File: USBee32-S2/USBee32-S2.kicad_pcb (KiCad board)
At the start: 4 copper layers, 27.9 x 68.4 mm, 52 parts, among them IC1 IP4220CZ6, J1 USB_A, J2 TYPE-C-31-M-12, J3 Conn_01x18_Male, J4 S2B-PH-SM4-TB(LF)(SN), J5 Conn_01x22_Male, SW1 SW_Push, SW2 SW_Push, U1 ESP32-S2-WROOM-ESP32-S2-WROOM, U2 MMBT8050, U3 MMBT8050, U4 MCP73831-2-OT, U5 AMS1117-3.3, U6 CH340C

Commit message: Rotated board
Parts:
- moved J3 76.8 mm to (203.8, 109.0), turned to 270 degrees
- moved J5 76.7 mm to (203.8, 133.8), turned to 270 degrees
- moved REF** 72.7 mm to (201.9, 114.8), turned to 90 degrees
- moved REF** 72.5 mm to (202.1, 124.1), turned to 90 degrees
- moved U1 64.1 mm to (196.2, 121.3), turned to 270 degrees
- moved GND 64.1 mm to (196.2, 120.1), turned to 270 degrees
- moved G1 55.3 mm to (190.1, 121.5), turned to 90 degrees
- moved G*** 46.9 mm to (184.1, 121.5), turned to 90 degrees
- moved R1 38.6 mm to (178.2, 121.4), turned to 90 degrees
- moved D2 35.6 mm to (174.9, 113.9), turned to 0 degrees
- moved C3 35.1 mm to (175.1, 115.9), turned to 0 degrees
- moved C8 34.5 mm to (175.0, 117.7), turned to 180 degrees
- moved C10 34.2 mm to (175.1, 119.4), turned to 180 degrees
- moved U5 31.7 mm to (173.1, 124.9), turned to 270 degrees
- moved R13 30.5 mm to (171.1, 113.9), turned to 180 degrees
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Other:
- board size 27.9 x 68.4 mm -> 68.4 x 27.9 mm

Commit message: Made suggested changes in schematics
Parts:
- removed G***: LOGO, USBee32-S2-Label:usbee32s2-qr
- removed G***: LOGO, USBee32-S2-Label:usbee32s2-fs
- removed G***: LOGO, USBee32-S2-Label:largelabel
- removed G1: LOGO, WS2018:sralogo
- removed GND: SolderWirePad_1x01_SMD_5x10mm, Connector_Wire:SolderWirePad_1x01_SMD_5x10mm
- removed the R11 at (153.1, 124.2)
- removed REF**: OSHW-Logo_5.7x6mm_SilkScreen, Designs:OSHW-Logo_5.7x6mm_SilkScreen
- removed REF**: KiCad-Logo_5mm_SilkScreen, Designs:KiCad-Logo_5mm_SilkScreen
- added R_PROG: 4.7k, Resistor_SMD:R_0603_1608Metric, F.Cu at (182.6, 108.7)
- moved J5 76.7 mm to (192.2, 58.0), turned to 0 degrees
- moved J3 62.6 mm to (167.4, 58.0), turned to 0 degrees
- moved U1 58.1 mm to (179.7, 65.5), turned to 0 degrees
- moved J1 50.1 mm to (188.9, 122.4), turned to 90 degrees
- moved D1 41.7 mm to (187.4, 112.9), turned to 180 degrees
- moved F1 40.4 mm to (187.3, 110.4), turned to 0 degrees
- moved D4 38.3 mm to (186.2, 94.6), turned to 0 degrees
- moved R1 37.8 mm to (179.8, 83.6), turned to 180 degrees
- moved U3 37.7 mm to (183.3, 88.7), turned to 0 degrees
- moved R4 36.6 mm to (185.6, 106.2), turned to 270 degrees
- moved C11 36.2 mm to (185.5, 99.2), turned to 90 degrees
- moved R9 36.1 mm to (185.6, 102.8), turned to 90 degrees
- moved J4 35.2 mm to (179.9, 116.7), turned to 0 degrees
- moved U2 35.0 mm to (182.8, 111.4), turned to 0 degrees
- moved C10 32.8 mm to (177.8, 86.7), turned to 270 degrees
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- renumbered U2 to Q1, U3 to Q2, R12 to R11, R13 to R12, R14 to R13, U4 to U2, U5 to U3, U6 to U4
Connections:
- net /GPIO0 renamed /GPIO_0
- net /GPIO1 renamed /GPIO_1
- net /GPIO10 renamed /GPIO_10
- net /GPIO11 renamed /GPIO_11
- net /GPIO12 renamed /GPIO_12
- net /GPIO13 renamed /GPIO_13
- net /GPIO14 renamed /GPIO_14
- net /GPIO15 renamed /GPIO_15
- net /GPIO16 renamed /GPIO_16
- net /GPIO17 renamed /GPIO_17
- net /GPIO18 renamed /GPIO_18
- net /GPIO19 renamed /GPIO_19
- net /GPIO2 renamed /GPIO_2
- net /GPIO20 renamed /GPIO_20
- net /GPIO21 renamed /GPIO_21
- net /GPIO26 renamed /GPIO_26
- net /GPIO3 renamed /GPIO_3
- net /GPIO33 renamed /GPIO_33
- net /GPIO34 renamed /GPIO_34
- net /GPIO35 renamed /GPIO_35
- net /GPIO36 renamed /GPIO_36
- net /GPIO37 renamed /GPIO_37
- net /GPIO38 renamed /GPIO_38
- net /GPIO39 renamed /GPIO_39
- net /GPIO4 renamed /GPIO_4
- net /GPIO40 renamed /GPIO_40
- net /GPIO41 renamed /GPIO_41
- net /GPIO42 renamed /GPIO_42
- net /GPIO45 renamed /GPIO_45
- net /GPIO46 renamed /GPIO_46
- net /GPIO5 renamed /GPIO_5
- net /GPIO6 renamed /GPIO_6
- net /GPIO7 renamed /GPIO_7
- net /GPIO8 renamed /GPIO_8
- net /GPIO9 renamed /GPIO_9
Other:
- board size 68.4 x 27.9 mm -> 27.9 x 68.4 mm

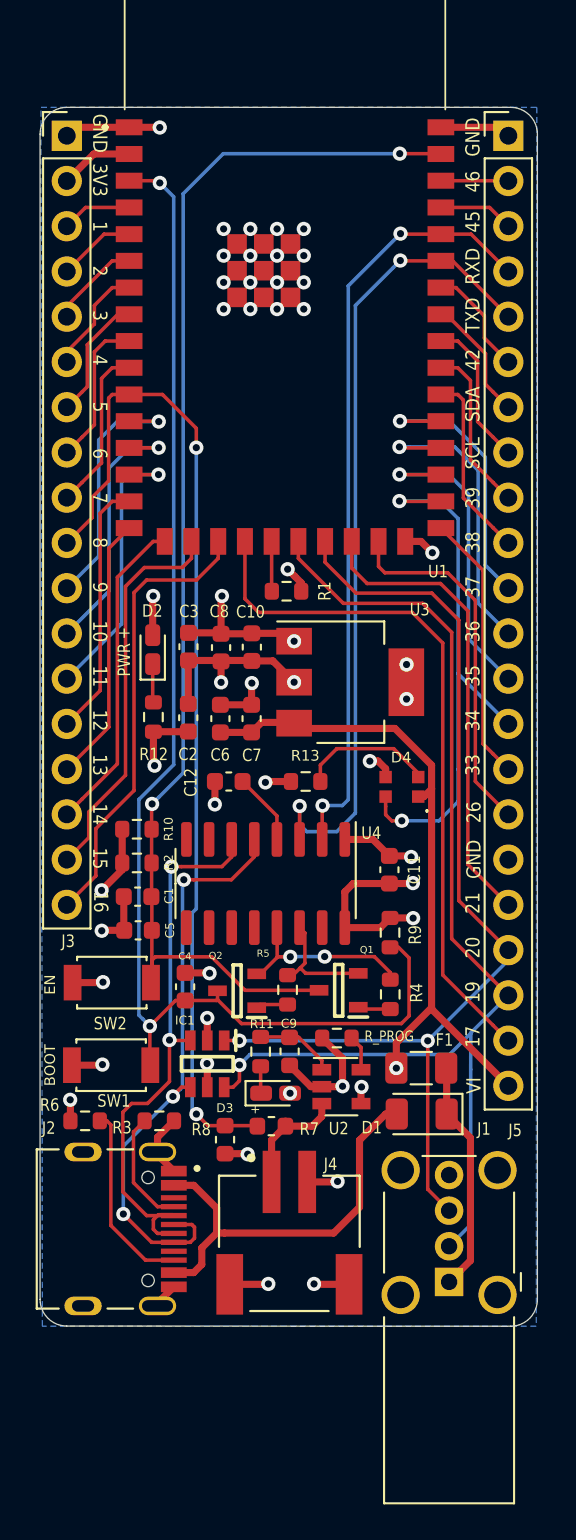
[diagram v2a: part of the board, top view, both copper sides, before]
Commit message: Rotated UsbC and added differential pair
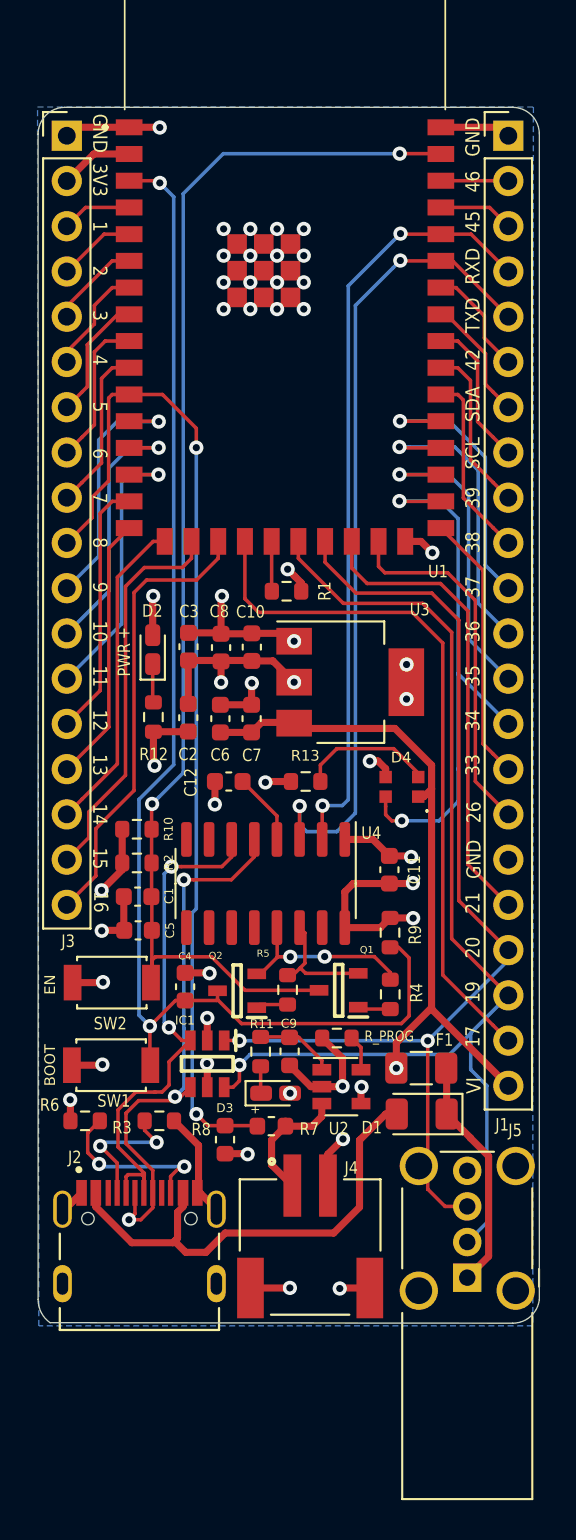
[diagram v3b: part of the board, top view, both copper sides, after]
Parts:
- moved J2 4.41 mm to (171.5, 122.5), turned to 0 degrees
- moved J4 1.18 mm to (181.1, 117.0)
- moved J1 1.05 mm to (189.9, 122.1)
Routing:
- net /VBUSC: track 23.3 -> 27.1 mm
- net GND: track 64.7 -> 68.2 mm
- net /DP1: track 33.5 -> 31.3 mm
- net /DN1: track 32.2 -> 30.0 mm
- net /CC1: track 6.55 -> 7.77 mm, vias 0 -> 2
- net /CC2: track 10.8 -> 9.80 mm, vias 0 -> 2
- net /GPIO_20: track 58.2 -> 59.1 mm
- net +BATT: track 7.86 -> 7.16 mm
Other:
- board size 27.9 x 68.4 mm -> 28.1 x 68.3 mm

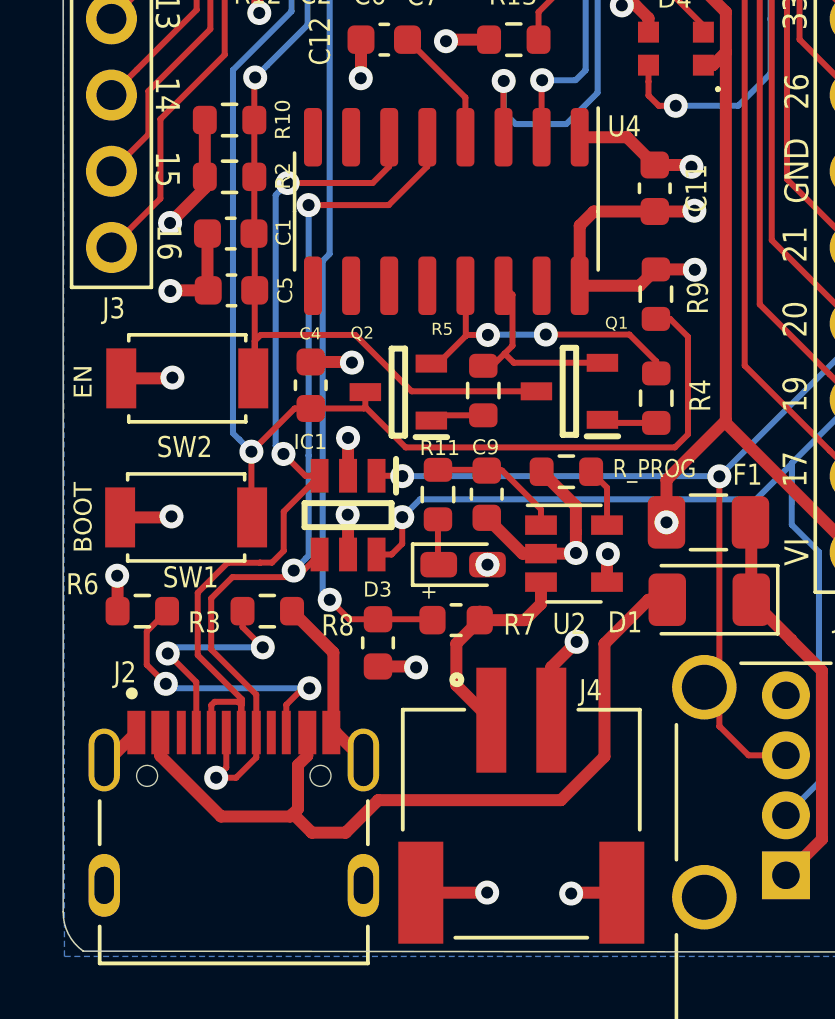
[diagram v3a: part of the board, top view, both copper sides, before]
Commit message: Made minor changes in routing
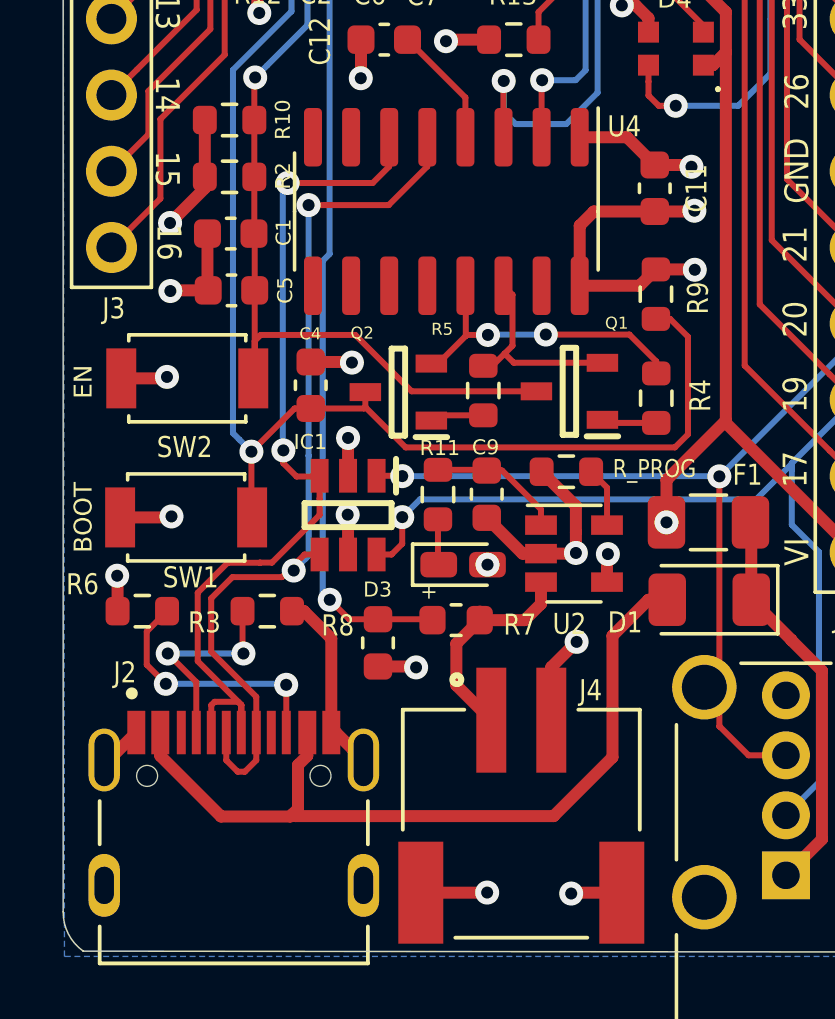
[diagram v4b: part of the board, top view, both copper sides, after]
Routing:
- net /CC2: track 9.80 -> 8.65 mm
- net /DP1: track 31.3 -> 30.3 mm, vias 3 -> 2
- net /CC1: track 7.77 -> 6.98 mm

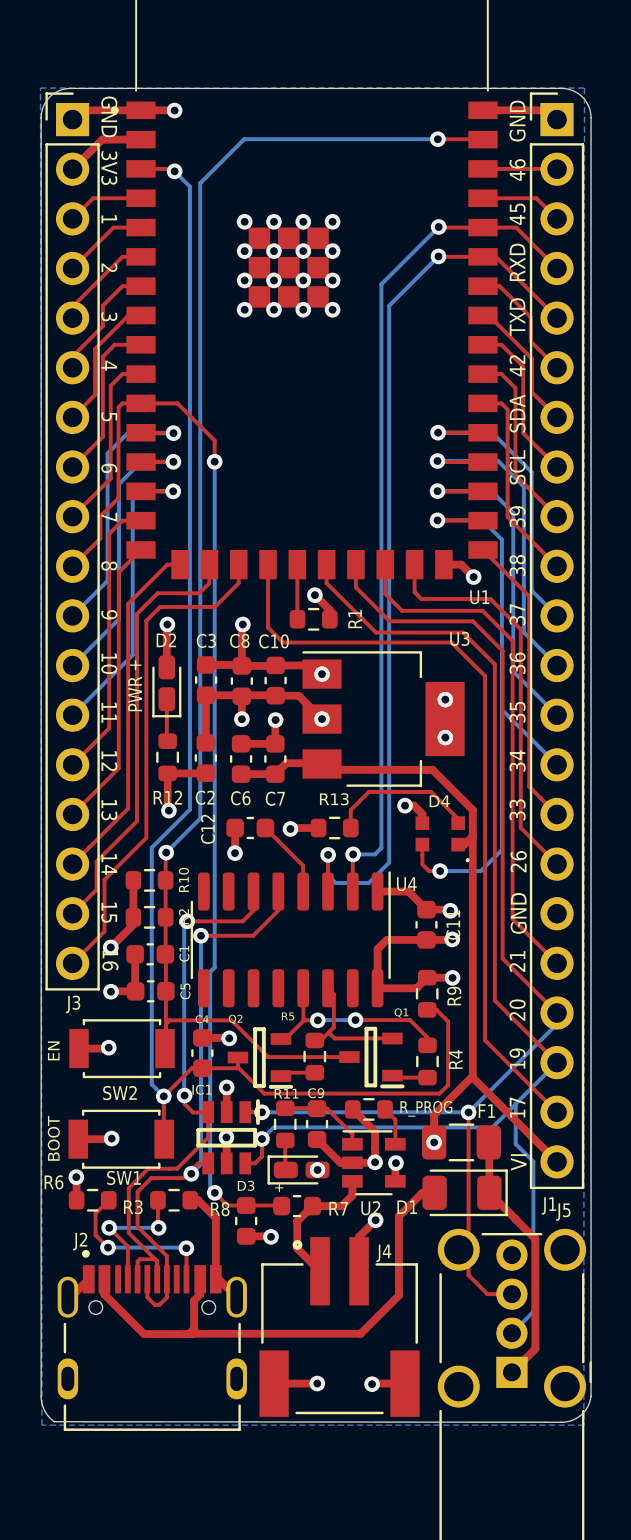
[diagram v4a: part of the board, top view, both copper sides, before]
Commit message: Added missing silkscreen and fixed edgecuts
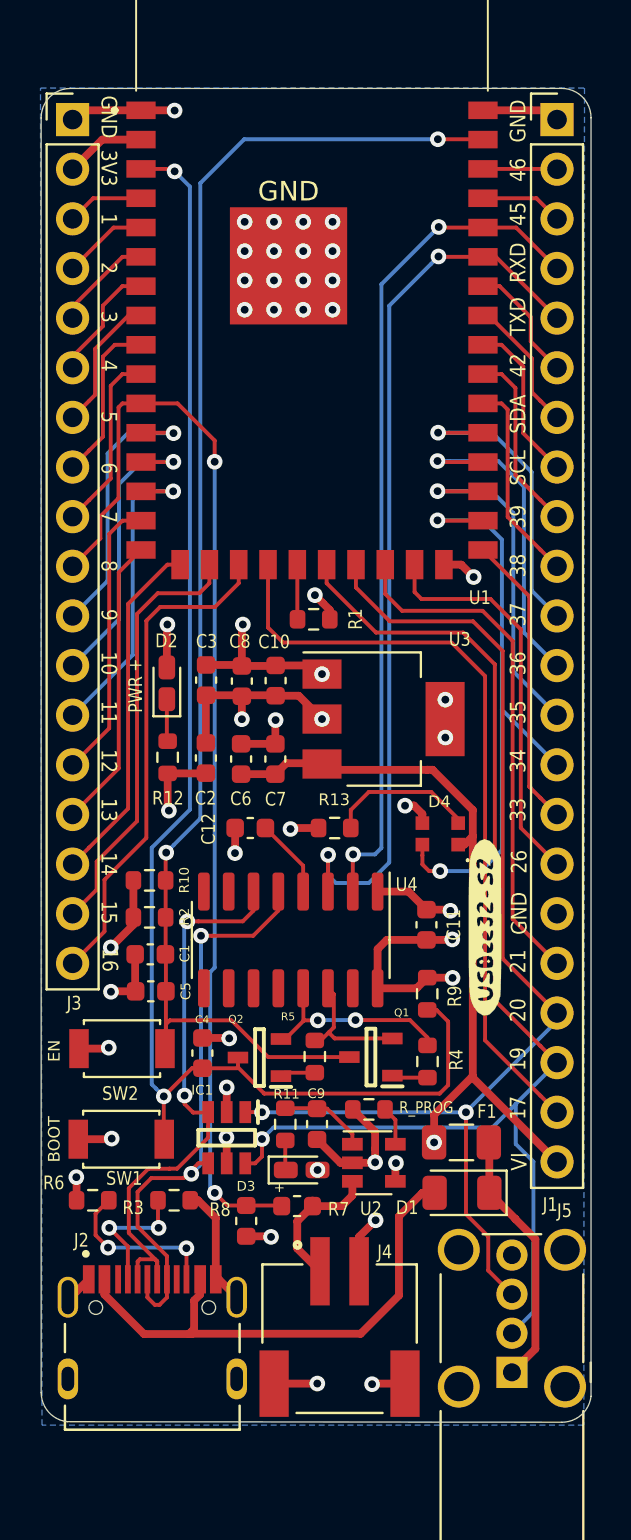
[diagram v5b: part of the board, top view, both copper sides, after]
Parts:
- added G***: LOGO, USBee32-S2-Label:usbee32s2-qr, B.Cu at (179.9, 90.2)
- added G***: LOGO, USBee32-S2-Label:largelabel, B.Cu at (179.6, 77.6)
- added G***: LOGO, WS2018:sralogo, B.Cu at (180.2, 72.1)
- added G***: LOGO, USBee32-S2-Label:usbee32s2-fs, F.Cu at (188.5, 99.4)
- added GND: SolderWirePad_1x01_SMD_5x10mm, Connector_Wire:SolderWirePad_1x01_SMD_5x10mm, F.Cu at (178.5, 65.5)
- added REF**: OSHW-Logo_5.7x6mm_SilkScreen, Designs:OSHW-Logo_5.7x6mm_SilkScreen, B.Cu at (172.9, 60.0)
- added REF**: KiCad-Logo_5mm_SilkScreen, Designs:KiCad-Logo_5mm_SilkScreen, B.Cu at (182.9, 59.8)
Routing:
- net /GPIO_20: track 59.1 -> 58.3 mm
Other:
- outline, holes or cut-outs redrawn

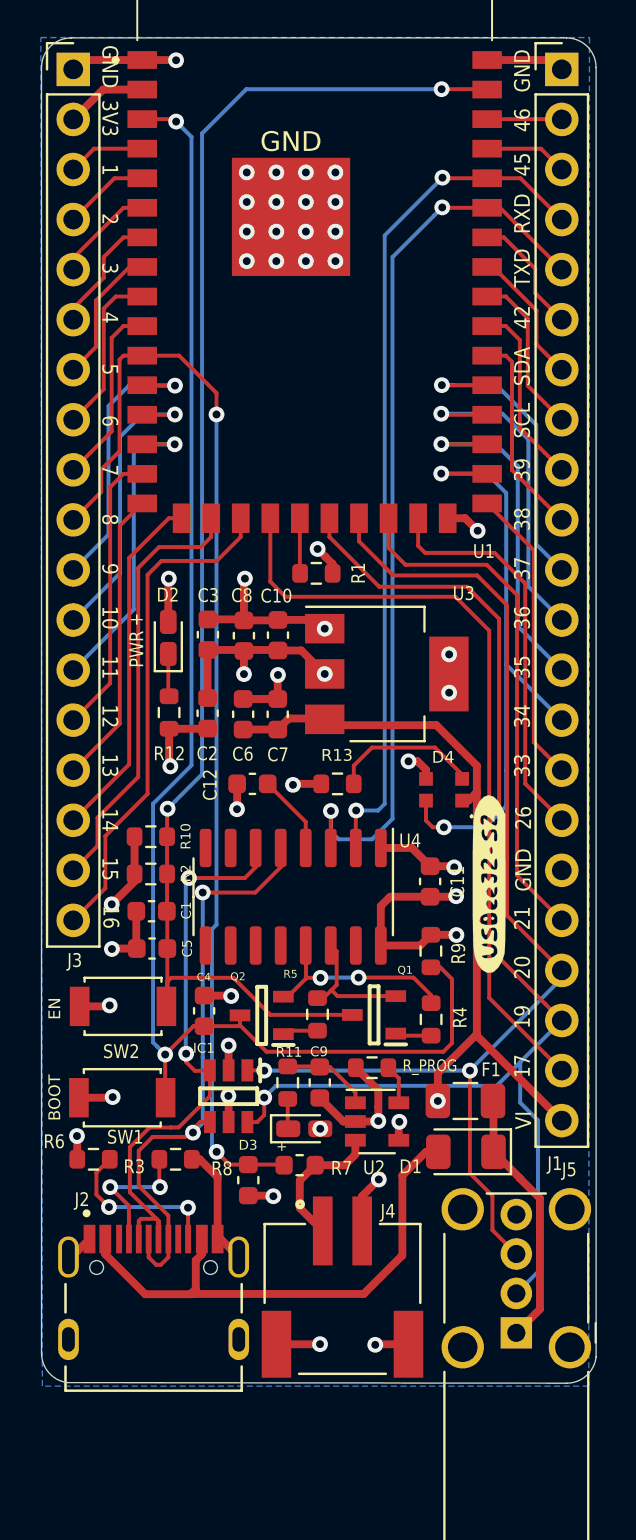
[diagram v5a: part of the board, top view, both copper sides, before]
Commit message: Made suggested routing, placement changes
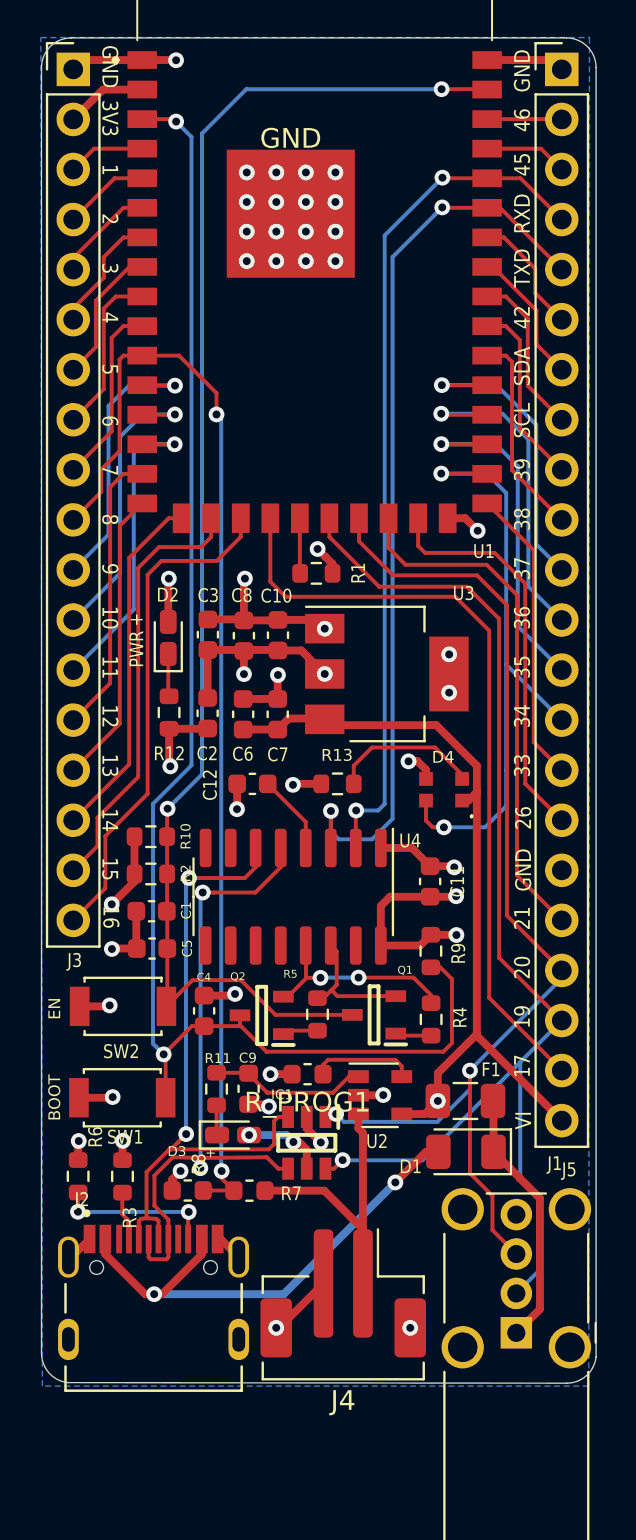
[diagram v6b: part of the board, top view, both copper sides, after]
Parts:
- removed G***: LOGO, USBee32-S2-Label:usbee32s2-qr
- removed G***: LOGO, USBee32-S2-Label:largelabel
- removed G***: LOGO, WS2018:sralogo
- removed G***: LOGO, USBee32-S2-Label:usbee32s2-fs
- removed REF**: OSHW-Logo_5.7x6mm_SilkScreen, Designs:OSHW-Logo_5.7x6mm_SilkScreen
- removed REF**: KiCad-Logo_5mm_SilkScreen, Designs:KiCad-Logo_5mm_SilkScreen
- removed R_PROG: 4.7k, Resistor_SMD:R_0603_1608Metric
- added R_PROG1: 4.7k, Resistor_SMD:R_0603_1608Metric, F.Cu at (179.3, 109.0)
- J4: footprint S2B-PH-SM4-TB_LF_SN:JST_S2B-PH-SM4-TB(LF)(SN) -> Connector_JST:JST_PH_B2B-PH-SM4-TB_1x02-1MP_P2.00mm_Vertical
- moved IC1 4.61 mm to (179.3, 112.5)
- moved D3 3.62 mm to (175.5, 112.1)
- moved C9 3.62 mm to (176.3, 109.7)
- moved R11 3.62 mm to (174.7, 109.8)
- moved J4 3.17 mm to (181.1, 120.1), turned to 180 degrees
- moved R8 3.12 mm to (173.2, 114.9), turned to 180 degrees
- moved R7 2.86 mm to (176.4, 114.9)
- moved R3 2.83 mm to (169.9, 114.2), turned to 90 degrees
- moved U2 1.34 mm to (183.0, 110.1)
- moved R6 1.16 mm to (167.7, 114.2), turned to 90 degrees
- moved GND 0.16 mm to (178.5, 65.3)
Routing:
- net +BATT: track 7.16 -> 17.2 mm
- net GND: track 68.2 -> 58.2 mm, vias 37 -> 39
- net /CC1: track 6.98 -> 2.50 mm, vias 2 -> 0
- net /VI: track 40.4 -> 44.3 mm, vias 4 -> 3
- net /DP1: track 30.3 -> 33.9 mm
- net /GPIO_19: track 64.2 -> 60.7 mm
- net Net-(C9-Pad1): track 4.51 -> 7.98 mm
- net Net-(R_PROG1-Pad1): track 2.00 -> 5.23 mm
- net /DN1: track 30.0 -> 33.1 mm
- net /GPIO_20: track 58.3 -> 56.2 mm
- net /VBUSC: track 26.8 -> 25.5 mm, vias 0 -> 2
- net /CHIP_PU: track 71.9 -> 71.1 mm
- net /CC2: track 8.65 -> 7.99 mm
